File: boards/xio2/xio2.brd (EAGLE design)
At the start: 170 x 100 mm, 376 parts, among them J1 12401598E4#2A, Q1 BSS138, Q2 BSS138, Q3 BC817-16LT3G, Q4 BC817-16LT3G, Y2 FA-238 25.0000MB-K3

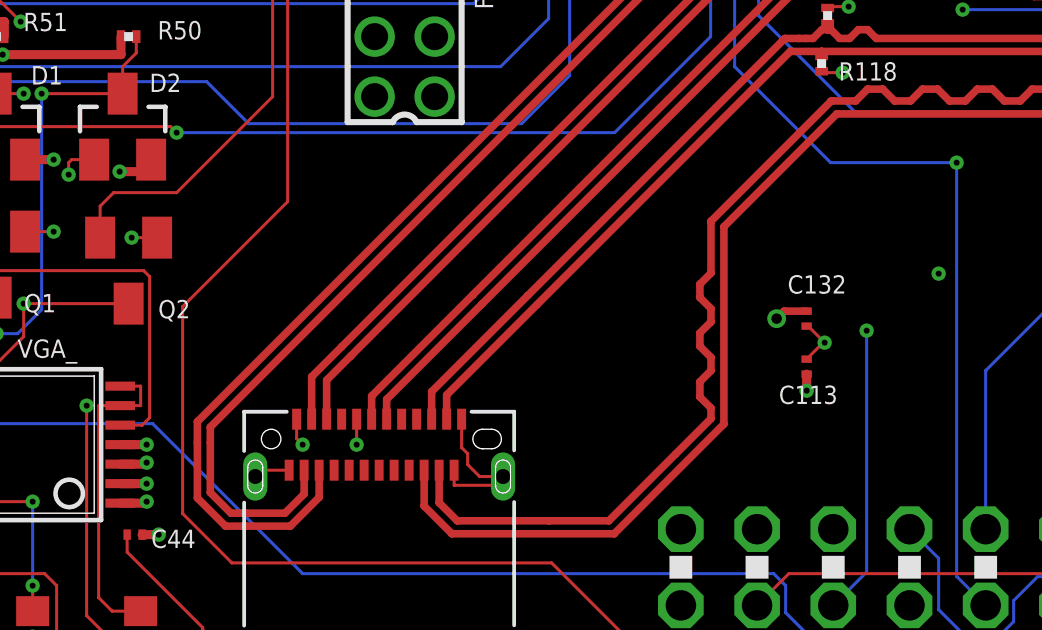
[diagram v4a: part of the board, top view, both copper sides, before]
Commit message: Move some things around on the board
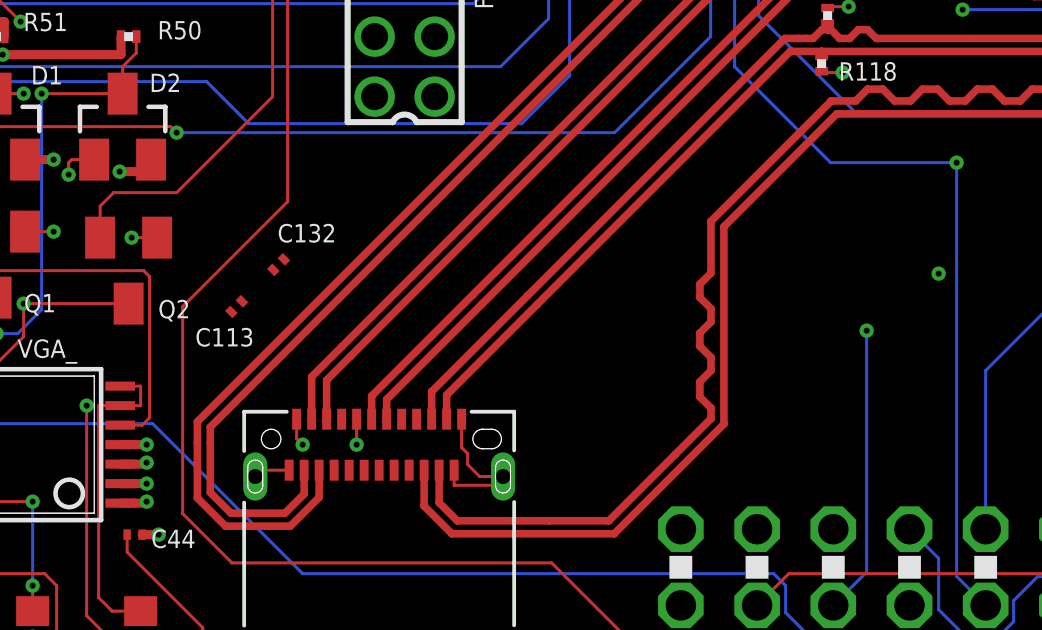
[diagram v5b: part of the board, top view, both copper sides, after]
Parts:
- moved C113 19.1 mm to (44.4, 15.0), turned to 45 degrees
- moved C132 17.7 mm to (45.8, 16.4), turned to 225 degrees
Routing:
- net GND: track 645.3 -> 643.7 mm, vias 362 -> 361
- net +3V3: track 260.3 -> 259.2 mm, vias 213 -> 212
- net +5V: track 104.1 -> 103.6 mm, vias 109 -> 108
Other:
- board text added: "Silkscreen needs work SDRAM ought to be length-matched QSPI ought to be length-matched SD Card ought to be length-matched Space for version label"
- board text removed: "Silkscreen needs work SDRAM ought to be length-matched QSPI ought to be length-matched SD Card ought to be length-matched Maybe rotate stm ccw by 90 degrees ?"
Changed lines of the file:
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@@
 <setting verticaltext="up"/>
 </settings>
-<grid distance="0.1" unitdist="mm" unit="mm" style="lines" multiple="1" display="yes" altdistance="1" altunitdist="mil" altunit="mil"/>
+<grid distance="0.0393700787" unitdist="inch" unit="inch" style="lines" multiple="1" display="yes" altdistance="1" altunitdist="mil" altunit="mil"/>
 <layers>
 <layer number="1" name="Top" color="4" fill="1" visible="yes" active="yes"/>
@@
 QSPI ought to be length-matched
 SD Card ought to be length-matched
-Maybe rotate stm ccw by 90 degrees ?</text>
+Space for version label</text>
 </plain>
 <attributes>
@@
 <attribute name="VALUE" x="36.705" y="24.565" size="1.27" layer="27" rot="R90"/>
 </element>
-<element name="C113" library="rcl" library_urn="urn:adsk.eagle:library:334" package="C0201" package3d_urn="urn:adsk.eagle:package:23690/2" value="0.1uF" x="63.4" y="13" locked="yes" smashed="yes" rot="R90">
-<attribute name="NAME" x="64.435" y="12.365" size="0.6096" layer="25" rot="R180"/>
-<attribute name="SPICEPREFIX" value="C" x="63.4" y="13" size="1.778" layer="27" rot="R90" display="off"/>
-<attribute name="USE" value="GRM033C71C104KE14D" x="63.4" y="13" size="1.778" layer="27" rot="R90" display="off"/>
-<attribute name="VALUE" x="65.305" y="12.365" size="1.27" layer="27" rot="R90"/>
+<element name="C113" library="rcl" library_urn="urn:adsk.eagle:library:334" package="C0201" package3d_urn="urn:adsk.eagle:package:23690/2" value="0.1uF" x="44.4" y="15" smashed="yes" rot="R45">
+<attribute name="NAME" x="44.980865625" y="14.282840625" size="0.6096" layer="25" rot="R180"/>
+<attribute name="SPICEPREFIX" value="C" x="44.4" y="15" size="1.778" layer="27" rot="R45" display="off"/>
+<attribute name="USE" value="GRM033C71C104KE14D" x="44.4" y="15" size="1.778" layer="27" rot="R45" display="off"/>
+<attribute name="VALUE" x="45.298025" y="13.20395" size="1.27" layer="27" rot="R45"/>
 </element>
 <element name="C114" library="rcl" library_urn="urn:adsk.eagle:library:334" package="C0201" package3d_urn="urn:adsk.eagle:package:23690/2" value="0.1uF" x="91.8" y="13.2" locked="yes" smashed="yes" rot="R90">
@@
 <attribute name="VALUE" x="133.365" y="29.295" size="1.27" layer="27"/>
 </element>
-<element name="C132" library="rcl" library_urn="urn:adsk.eagle:library:334" package="C0201" package3d_urn="urn:adsk.eagle:package:23690/2" value="0.1uF" x="63.4" y="14.6" locked="yes" smashed="yes" rot="R270">
-<attribute name="NAME" x="62.765" y="15.435" size="0.6096" layer="25"/>
-<attribute name="SPICEPREFIX" value="C" x="33.4" y="14.6" size="1.778" layer="27" rot="R270" display="off"/>
-<attribute name="USE" value="GRM033C71C104KE14D" x="63.4" y="14.6" size="1.778" layer="27" rot="R270" display="off"/>
-<attribute name="VALUE" x="61.495" y="15.235" size="1.27" layer="27" rot="R270"/>
+<element name="C132" library="rcl" library_urn="urn:adsk.eagle:library:334" package="C0201" package3d_urn="urn:adsk.eagle:package:23690/2" value="0.1uF" x="45.8" y="16.4" smashed="yes" rot="R225">
+<attribute name="NAME" x="45.76055" y="17.14141875" size="0.6096" layer="25"/>
+<attribute name="SPICEPREFIX" value="C" x="24.586796875" y="37.61320625" size="1.778" layer="27" rot="R225" display="off"/>
+<attribute name="USE" value="GRM033C71C104KE14D" x="45.8" y="16.4" size="1.778" layer="27" rot="R225" display="off"/>
+<attribute name="VALUE" x="44.901971875" y="18.196053125" size="1.27" layer="27" rot="R225"/>
 </element>
 <element name="C133" library="rcl" library_urn="urn:adsk.eagle:library:334" package="C0201" package3d_urn="urn:adsk.eagle:package:23690/2" value="0.1uF" x="35.8" y="26.4" locked="yes" smashed="yes" rot="R180">
@@
 <element name="POWER" library="sjg-power" package="DCJ3P-14.2X11.0X9.0MM" value="dc5vin" x="154" y="7.1" locked="yes" smashed="yes" rot="R90">
 <attribute name="MPN" value="DC-005" x="154" y="7.1" size="1.778" layer="27" rot="R90" display="off"/>
-<attribute name="NAME" x="154.635" y="7.1" size="0.254" layer="33" ratio="10" rot="R180"/>
 <attribute name="NAME" x="159.99" y="1.775" size="0.6096" layer="25" ratio="11" rot="R90"/>
+<attribute name="NAME" x="154.635" y="7.1" size="0.254" layer="33" ratio="10" rot="R180"/>
 <attribute name="USE" value="PJ-102AH" x="154" y="7.1" size="1.778" layer="27" rot="R90" display="off"/>
 <attribute name="VALUE" x="154.635" y="-2.425" size="0.889" layer="27" ratio="11" rot="R90"/>
@@
 <via x="31.5" y="49.1" extent="1-16" drill="0.2" diameter="0.4794"/>
 <via x="24.3" y="49.1" extent="1-16" drill="0.2" diameter="0.4794"/>
-<via x="64" y="13.8" extent="1-16" drill="0.2" diameter="0.4794"/>
-<wire x1="63.4" y1="14.35" x2="63.45" y2="14.35" width="0.1016" layer="1"/>
-<wire x1="63.45" y1="14.35" x2="64" y2="13.8" width="0.1016" layer="1"/>
-<wire x1="63.4" y1="13.25" x2="63.95" y2="13.8" width="0.1016" layer="1"/>
-<wire x1="63.95" y1="13.8" x2="64" y2="13.8" width="0.1016" layer="1"/>
 <wire x1="124.4" y1="7.5" x2="124.1" y2="7.2" width="0.1016" layer="1"/>
 <wire x1="124.1" y1="7.2" x2="124" y2="7.2" width="0.1016" layer="1"/>
@@
 <wire x1="32.9" y1="44.2" x2="32.9" y2="44.1" width="0.1016" layer="1"/>
 <wire x1="32.9864" y1="44.2864" x2="32.9864" y2="44.575" width="0.1016" layer="1"/>
+<wire x1="44.576775" y1="15.176775" x2="45.623221875" y2="16.223221875" width="0" layer="19" extent="1-1"/>
+<wire x1="46.4" y1="11.2475" x2="44.576775" y2="15.176775" width="0" layer="19" extent="1-1"/>
 </signal>
 <signal name="+3V3" class="9">
@@
 <contactref element="C133" pad="1"/>
 <contactref element="C138" pad="1"/>
-<via x="62.4" y="14.6" extent="1-16" drill="0.35" locked="yes"/>
-<wire x1="63.4" y1="14.85" x2="62.65" y2="14.85" width="0.254" layer="1" locked="yes"/>
-<wire x1="62.65" y1="14.85" x2="62.4" y2="14.6" width="0.254" layer="1" locked="yes"/>
 <contactref element="C146" pad="1"/>
 <contactref element="C145" pad="1"/>
@@
 <wire x1="54.055" y1="28" x2="54.055" y2="29.5" width="0.1016" layer="1"/>
 <wire x1="54.055" y1="28" x2="54.055" y2="26" width="0.1016" layer="1"/>
+<wire x1="41.75" y1="17.3" x2="45.976775" y2="16.576775" width="0" layer="19" extent="1-1"/>
 </signal>
 <signal name="+5V" class="1">
@@
 <wire x1="26.6" y1="32" x2="26.6" y2="32.55" width="0.3048" layer="1"/>
 <wire x1="34.8" y1="24.4" x2="34.8" y2="24.95" width="0.3048" layer="1"/>
-<wire x1="63.4" y1="12.2" x2="63.4" y2="12.75" width="0.3048" layer="1"/>
 <wire x1="91.8" y1="12.4" x2="91.8" y2="12.95" width="0.3048" layer="1"/>
 <wire x1="106" y1="12.4" x2="106" y2="12.95" width="0.3048" layer="1"/>
@@
 <via x="26.6" y="32" extent="1-16" drill="0.2032" diameter="0.4826"/>
 <via x="34.8" y="24.4" extent="1-16" drill="0.2032" diameter="0.4826"/>
-<via x="63.4" y="12.2" extent="1-16" drill="0.2032" diameter="0.4826"/>
 <via x="91.8" y="12.4" extent="1-16" drill="0.2032" diameter="0.4826"/>
 <via x="106" y="12.4" extent="1-16" drill="0.2032" diameter="0.4826"/>
@@
 <via x="113.5" y="90.2" extent="1-16" drill="0.2032" diameter="0.4826"/>
 <via x="75.4" y="89.5" extent="1-16" drill="0.2032" diameter="0.4826"/>
+<wire x1="41.4" y1="10.4" x2="44.223221875" y2="14.823221875" width="0" layer="19" extent="1-1"/>
 </signal>
 <signal name="!RESET!">

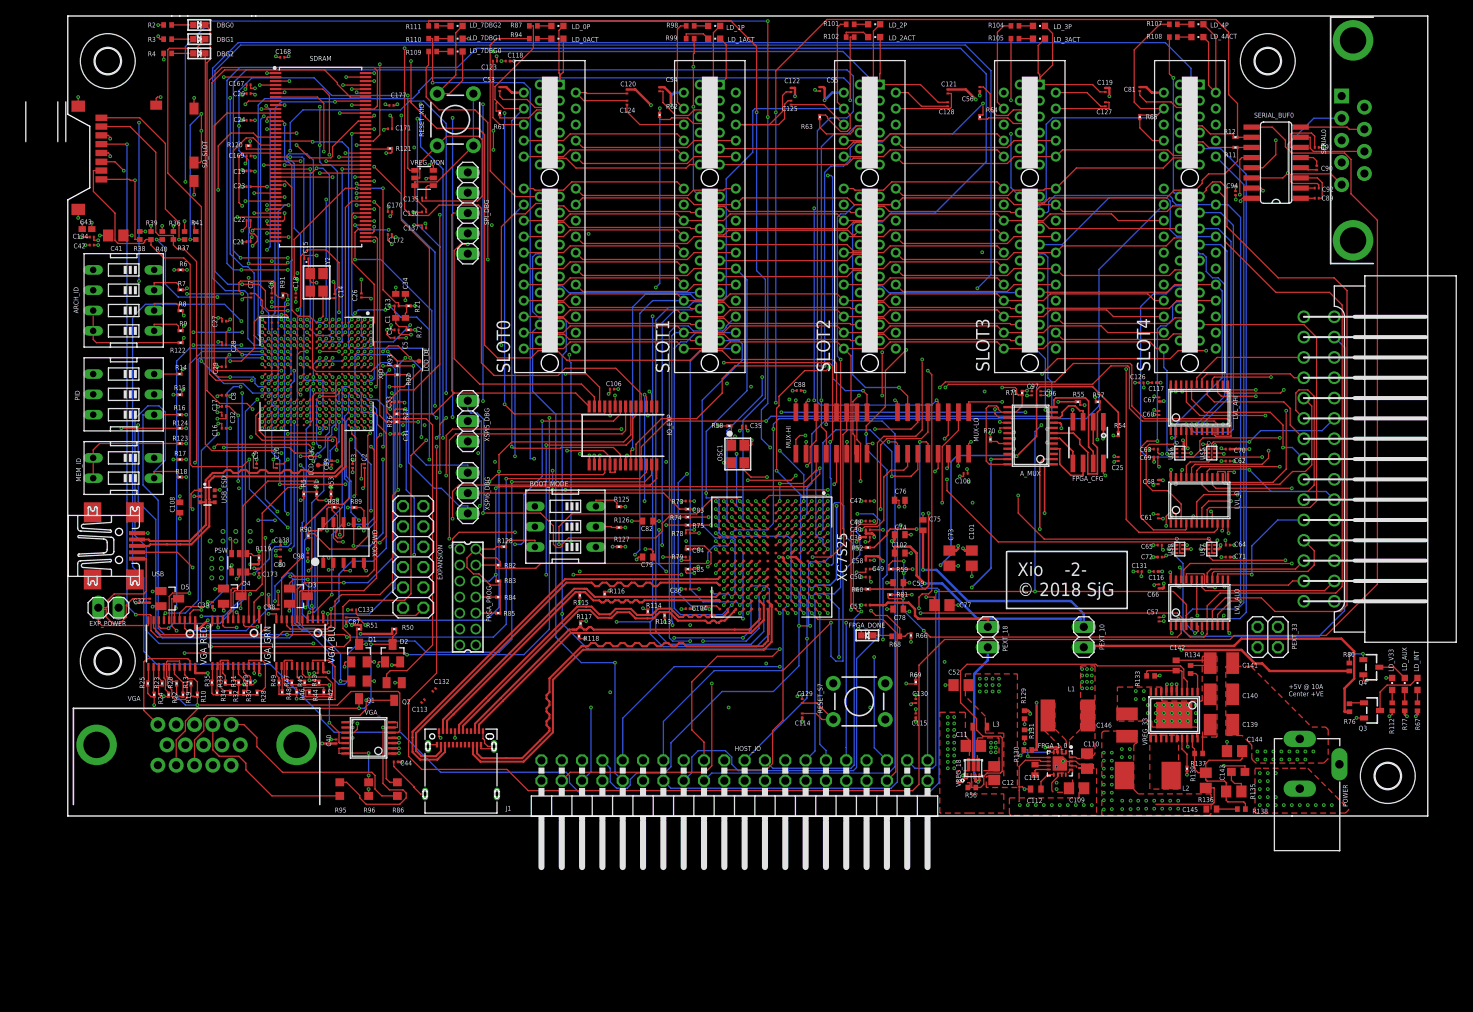
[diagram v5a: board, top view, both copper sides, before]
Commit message: Some minor changes in layout
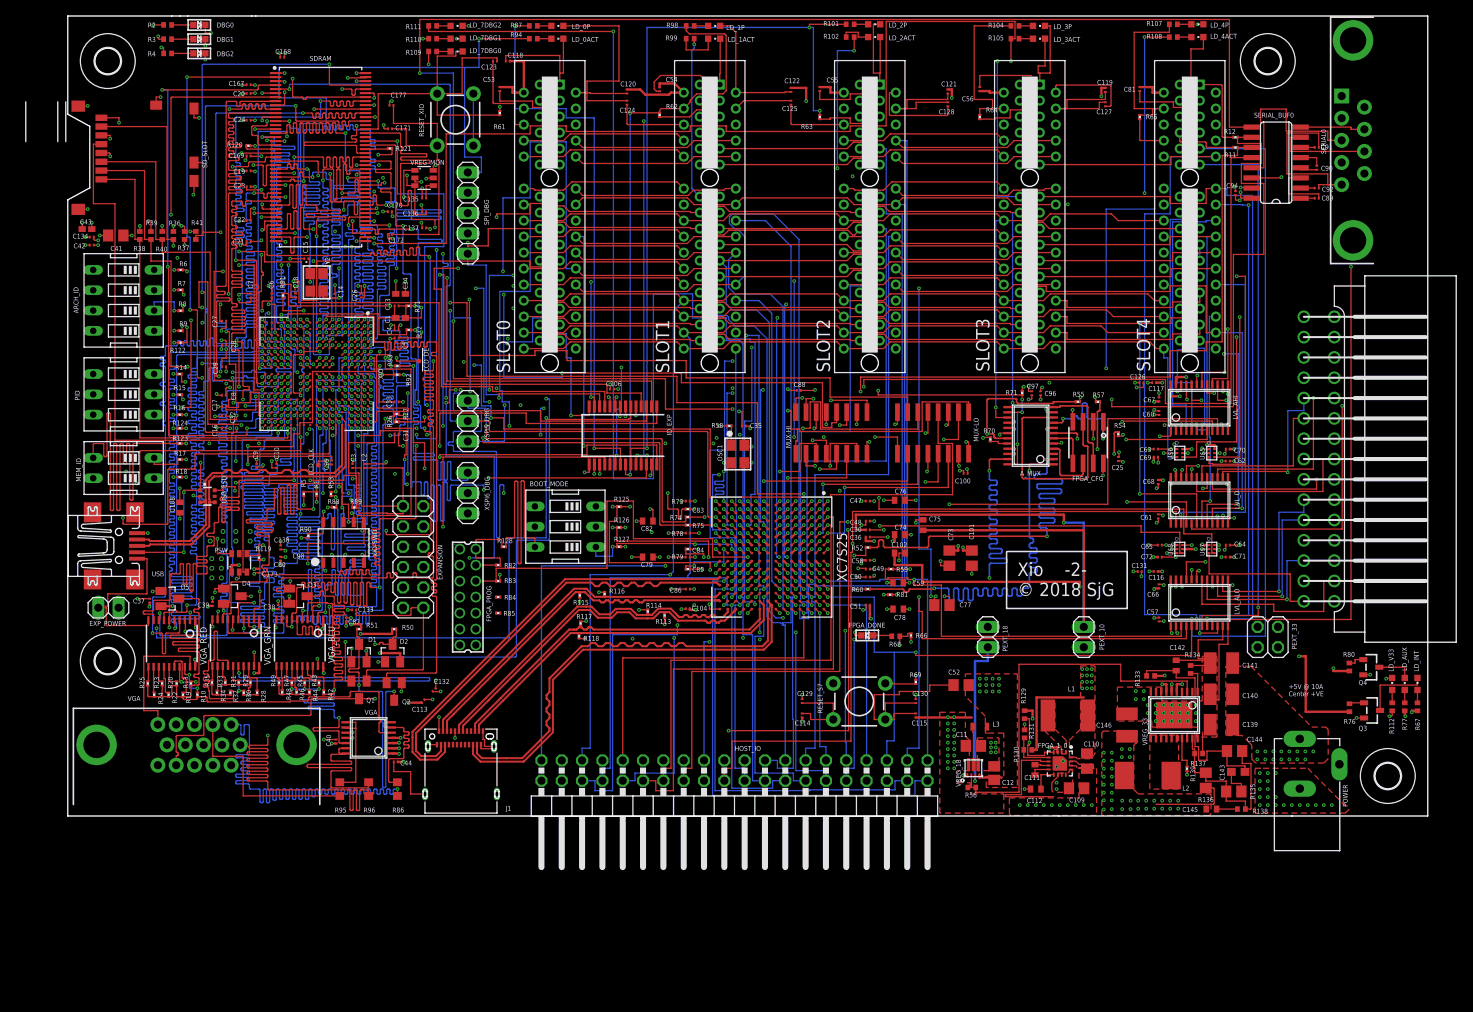
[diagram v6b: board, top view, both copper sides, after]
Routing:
- net GND: track 643.7 -> 799.5 mm, vias 361 -> 353
- net SDRAM_BA1: track 37.9 -> 169.5 mm, vias 2 -> 4
- net STM_MUX_CTL: track 221.7 -> 104.7 mm, vias 6 -> 4
- net HOST_A0: track 405.4 -> 296.5 mm, vias 7 -> 4
- net STM_MUX_D1: track 200.3 -> 100.6 mm, vias 4 -> 2
- net STM_MUX_D3: track 216.3 -> 125.6 mm, vias 3 -> 2
- net !ADDR_VALID_WRITE!: track 193.3 -> 103.9 mm, vias 6 -> 4
- net MCU_CTS: track 266.8 -> 185.4 mm
- net STM_MUX_D4: track 180.0 -> 108.5 mm, vias 5 -> 2
- net STM_MUX_D7: track 167.6 -> 97.6 mm, vias 4 -> 3
- net SDRAM_BA0: track 37.8 -> 106.8 mm, vias 2 -> 4
- net LCD_B2: track 33.0 -> 101.3 mm, vias 2 -> 3
- net N$48: track 14.4 -> 80.0 mm
- net HOST_A12: track 318.0 -> 252.5 mm, vias 8 -> 5
- net STM_MUX_D0: track 182.2 -> 116.9 mm, vias 5 -> 3
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
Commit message: Text changes
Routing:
- net SPI_IRQ2: track 114.6 -> 111.0 mm
- net N$92: track 5.55 -> 4.73 mm
- net SPI_SS1: track 112.0 -> 111.3 mm
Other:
- board text added: "Silkscreen needs work Space for version label"
- board text removed: "Silkscreen needs work SDRAM ought to be length-matched QSPI ought to be length-matched SD Card ought to be length-matched Space for version label"
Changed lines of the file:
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@@
 <setting verticaltext="up"/>
 </settings>
-<grid distance="0.1" unitdist="mm" unit="mm" style="lines" multiple="1" display="yes" altdistance="1" altunitdist="mil" altunit="mil"/>
+<grid distance="1" unitdist="mil" unit="mil" style="lines" multiple="1" display="yes" altdistance="1" altunitdist="mil" altunit="mil"/>
 <layers>
 <layer number="1" name="Top" color="4" fill="1" visible="yes" active="yes"/>
@@
 <text x="152.6" y="15.6" locked="yes" size="0.6096" layer="25">+5V @ 10A
 Center +VE</text>
-<text x="71.05" y="-14.2" locked="yes" size="0.6096" layer="50">Silkscreen needs work
-SDRAM ought to be length-matched
-QSPI ought to be length-matched
-SD Card ought to be length-matched
+<text x="77.55" y="-11.5" size="0.6096" layer="50">Silkscreen needs work
 Space for version label</text>
 </plain>
@@
 <wire x1="25.5" y1="60.3" x2="25.5" y2="85.1" width="0.1016" layer="16"/>
 <wire x1="25.5" y1="85.1" x2="24.9" y2="85.1" width="0.1016" layer="16"/>
-<wire x1="78.3" y1="97.1" x2="78.3" y2="96.2" width="0.1016" layer="3"/>
-<wire x1="78.3" y1="96.2" x2="38.8" y2="96.2" width="0.1016" layer="3"/>
+<wire x1="78.3" y1="97.1" x2="78.3" y2="96.2127" width="0.1016" layer="3"/>
+<wire x1="78.3" y1="96.2127" x2="78.2873" y2="96.2" width="0.1016" layer="3" curve="-90"/>
+<wire x1="78.2873" y1="96.2" x2="38.8" y2="96.2" width="0.1016" layer="3"/>
 <wire x1="38.8" y1="96.2" x2="38.8" y2="86.4" width="0.1016" layer="3"/>
-<wire x1="38.8" y1="86.4" x2="24.9" y2="86.4" width="0.1016" layer="3"/>
-<wire x1="24.9" y1="86.4" x2="24.9" y2="85.1" width="0.1016" layer="3"/>
 <wire x1="78.3" y1="97.1" x2="78.3" y2="97.8" width="0.1016" layer="1"/>
 <wire x1="25.1" y1="60.3" x2="25.5" y2="59.9" width="0.1016" layer="1"/>
@@
 <via x="78.3" y="97.1" extent="1-16" drill="0.2" diameter="0.4794"/>
 <via x="25.1" y="60.3" extent="1-16" drill="0.2" diameter="0.4794"/>
+<wire x1="38.8" y1="86.4" x2="26.2" y2="86.4" width="0.1016" layer="3"/>
+<wire x1="26.2" y1="86.4" x2="24.9" y2="85.1" width="0.1016" layer="3"/>
 </signal>
 <signal name="SPI_SS2" class="11">
@@
 <wire x1="90.8" y1="47.2" x2="90.8" y2="48" width="0.1016" layer="3"/>
 <wire x1="90.8" y1="67.5" x2="90.8" y2="48" width="0.1016" layer="16"/>
-<wire x1="90.8" y1="67.5" x2="90.8" y2="77.06" width="0.1016" layer="14"/>
-<wire x1="90.8" y1="77.06" x2="97" y2="77.06" width="0.1016" layer="14"/>
 <wire x1="81" y1="36" x2="81.5" y2="35.5" width="0.1016" layer="1"/>
 <wire x1="37.9" y1="54.7" x2="37.5" y2="55.1" width="0.1016" layer="1"/>
@@
 <via x="81" y="36" extent="1-16" drill="0.2" diameter="0.4794"/>
 <via x="37.9" y="54.7" extent="1-16" drill="0.2" diameter="0.4794"/>
+<wire x1="90.8" y1="67.5" x2="90.8" y2="70.86" width="0.1016" layer="14"/>
+<wire x1="90.8" y1="70.86" x2="97" y2="77.06" width="0.1016" layer="14"/>
 </signal>
 <signal name="SPI_IRQ3" class="11">
@@
 <wire x1="92.7" y1="99.2" x2="92.7" y2="99.6" width="0.1016" layer="1"/>
 <wire x1="92.7" y1="99.6" x2="97.3" y2="99.6" width="0.1016" layer="1"/>
-<wire x1="72.4" y1="46.6" x2="72.4" y2="99.2" width="0.1016" layer="16"/>
-<wire x1="72.4" y1="99.2" x2="92.7" y2="99.2" width="0.1016" layer="16"/>
+<wire x1="72.4" y1="46.6" x2="72.4" y2="99.1873" width="0.1016" layer="16"/>
+<wire x1="72.4" y1="99.1873" x2="72.4127" y2="99.2" width="0.1016" layer="16" curve="-90"/>
+<wire x1="72.4127" y1="99.2" x2="92.7" y2="99.2" width="0.1016" layer="16"/>
 <wire x1="92.7" y1="99.2" x2="93.2" y2="99.2" width="0.1016" layer="16"/>
 <wire x1="72.4" y1="46.6" x2="70.375" y2="46.6" width="0.1016" layer="1"/>
@@
 <contactref element="LD_1ACT" pad="A"/>
 <wire x1="77.3" y1="97.8" x2="77.3" y2="96.4" width="0.1016" layer="1"/>
-<wire x1="77.3" y1="96.4" x2="80.05" y2="96.4" width="0.1016" layer="1"/>
-<wire x1="80.05" y1="96.4" x2="80.05" y2="97.8" width="0.1016" layer="1"/>
+<wire x1="77.3" y1="96.4" x2="78.65" y2="96.4" width="0.1016" layer="1"/>
+<wire x1="78.65" y1="96.4" x2="80.05" y2="97.8" width="0.1016" layer="1"/>
 </signal>
 <signal name="N$94">
